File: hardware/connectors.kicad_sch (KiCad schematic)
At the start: 23 parts, among them J1 Kenwood-2.5, J10 UART, J11 Radio_Opt, J12 Speaker, J13 8P8C_Shielded, J2 USB_C, J301 +12V, J5 Kenwood-3.5, J7 Radio, J9 STLink, U3 USBLC6-2

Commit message: Modified components references
Modified references to fit the previous references (from before adding the new sheets)
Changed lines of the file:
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@@
   (symbol (lib_id "Connector:8P8C_Shielded") (at 70.485 43.815 0) (unit 1)
     (in_bom yes) (on_board yes) (dnp no) (fields_autoplaced)
-    (property "Reference" "J13" (at 70.485 26.035 0)
-      (effects (font (size 1.27 1.27)))
-    )
-    (property "Value" "8P8C_Shielded" (at 70.485 28.575 0)
+    (property "Reference" "J13" (at 70.485 26.67 0)
+      (effects (font (size 1.27 1.27)))
+    )
+    (property "Value" "8P8C_Shielded" (at 70.485 29.21 0)
       (effects (font (size 1.27 1.27)))
     )
@@
         )
         (path "/59592280-3207-432b-a891-cd517ec5cf12/7f9420e4-5dd1-4e05-8205-18dae2029540"
-          (reference "J402") (unit 1)
+          (reference "J13") (unit 1)
         )
       )
@@
         )
         (path "/59592280-3207-432b-a891-cd517ec5cf12/7f9420e4-5dd1-4e05-8205-18dae2029540"
-          (reference "R406") (unit 1)
+          (reference "R16") (unit 1)
         )
       )
@@
         )
         (path "/59592280-3207-432b-a891-cd517ec5cf12/7f9420e4-5dd1-4e05-8205-18dae2029540"
-          (reference "C401") (unit 1)
+          (reference "C32") (unit 1)
         )
       )
@@
         )
         (path "/59592280-3207-432b-a891-cd517ec5cf12/7f9420e4-5dd1-4e05-8205-18dae2029540"
-          (reference "R403") (unit 1)
+          (reference "R34") (unit 1)
         )
       )
@@
   (symbol (lib_id "Diode:BAT60A") (at 191.77 35.56 180) (unit 1)
     (in_bom yes) (on_board yes) (dnp no) (fields_autoplaced)
-    (property "Reference" "D9" (at 191.77 30.3234 0)
-      (effects (font (size 1.27 1.27)))
-    )
-    (property "Value" "BAT60A" (at 191.77 33.0985 0)
+    (property "Reference" "D9" (at 192.0875 29.21 0)
+      (effects (font (size 1.27 1.27)))
+    )
+    (property "Value" "BAT60A" (at 192.0875 31.75 0)
       (effects (font (size 1.27 1.27)))
     )
@@
         )
         (path "/59592280-3207-432b-a891-cd517ec5cf12/7f9420e4-5dd1-4e05-8205-18dae2029540"
-          (reference "D401") (unit 1)
+          (reference "D9") (unit 1)
         )
       )
@@
         )
         (path "/59592280-3207-432b-a891-cd517ec5cf12/7f9420e4-5dd1-4e05-8205-18dae2029540"
-          (reference "R401") (unit 1)
+          (reference "R70") (unit 1)
         )
       )
@@
   (symbol (lib_id "Connector:Barrel_Jack_Switch_Pin3Ring") (at 120.65 161.29 0) (unit 1)
     (in_bom yes) (on_board yes) (dnp no) (fields_autoplaced)
-    (property "Reference" "J301" (at 122.047 153.5134 0)
-      (effects (font (size 1.27 1.27)))
-    )
-    (property "Value" "+12V" (at 122.047 156.2885 0)
+    (property "Reference" "J301" (at 120.65 152.4 0)
+      (effects (font (size 1.27 1.27)))
+    )
+    (property "Value" "+12V" (at 120.65 154.94 0)
       (effects (font (size 1.27 1.27)))
     )
@@
         )
         (path "/59592280-3207-432b-a891-cd517ec5cf12/7f9420e4-5dd1-4e05-8205-18dae2029540"
-          (reference "J410") (unit 1)
+          (reference "J8") (unit 1)
         )
       )
@@
         )
         (path "/59592280-3207-432b-a891-cd517ec5cf12/7f9420e4-5dd1-4e05-8205-18dae2029540"
-          (reference "J401") (unit 1)
+          (reference "J7") (unit 1)
         )
       )
@@
         )
         (path "/59592280-3207-432b-a891-cd517ec5cf12/7f9420e4-5dd1-4e05-8205-18dae2029540"
-          (reference "R404") (unit 1)
+          (reference "R35") (unit 1)
         )
       )
@@
   (symbol (lib_id "Connector_Generic:Conn_01x03") (at 180.34 129.54 0) (unit 1)
     (in_bom no) (on_board yes) (dnp yes) (fields_autoplaced)
-    (property "Reference" "J10" (at 182.3721 128.6315 0)
+    (property "Reference" "J10" (at 182.88 128.27 0)
       (effects (font (size 1.27 1.27)) (justify left))
     )
-    (property "Value" "UART" (at 182.3721 131.4066 0)
+    (property "Value" "UART" (at 182.88 130.81 0)
       (effects (font (size 1.27 1.27)) (justify left))
     )
@@
         )
         (path "/59592280-3207-432b-a891-cd517ec5cf12/7f9420e4-5dd1-4e05-8205-18dae2029540"
-          (reference "J409") (unit 1)
+          (reference "J10") (unit 1)
         )
       )
@@
   (symbol (lib_id "Connector_Generic:Conn_01x06") (at 109.22 109.22 0) (unit 1)
     (in_bom yes) (on_board yes) (dnp no) (fields_autoplaced)
-    (property "Reference" "J11" (at 111.76 109.2199 0)
+    (property "Reference" "J11" (at 111.76 109.22 0)
       (effects (font (size 1.27 1.27)) (justify left))
     )
-    (property "Value" "Radio_Opt" (at 111.76 111.7599 0)
+    (property "Value" "Radio_Opt" (at 111.76 111.76 0)
       (effects (font (size 1.27 1.27)) (justify left))
     )
@@
         )
         (path "/59592280-3207-432b-a891-cd517ec5cf12/7f9420e4-5dd1-4e05-8205-18dae2029540"
-          (reference "J405") (unit 1)
+          (reference "J11") (unit 1)
         )
       )
@@
         )
         (path "/59592280-3207-432b-a891-cd517ec5cf12/7f9420e4-5dd1-4e05-8205-18dae2029540"
-          (reference "J403") (unit 1)
+          (reference "J1") (unit 1)
         )
       )
@@
         )
         (path "/59592280-3207-432b-a891-cd517ec5cf12/7f9420e4-5dd1-4e05-8205-18dae2029540"
-          (reference "R407") (unit 1)
+          (reference "R28") (unit 1)
         )
       )
@@
   (symbol (lib_id "Connector_Generic:Conn_01x02") (at 61.595 149.225 0) (unit 1)
     (in_bom no) (on_board yes) (dnp yes) (fields_autoplaced)
-    (property "Reference" "J12" (at 64.135 149.2249 0)
+    (property "Reference" "J12" (at 64.77 149.225 0)
       (effects (font (size 1.27 1.27)) (justify left))
     )
-    (property "Value" "Speaker" (at 64.135 151.7649 0)
+    (property "Value" "Speaker" (at 64.77 151.765 0)
       (effects (font (size 1.27 1.27)) (justify left))
     )
@@
         )
         (path "/59592280-3207-432b-a891-cd517ec5cf12/7f9420e4-5dd1-4e05-8205-18dae2029540"
-          (reference "J407") (unit 1)
+          (reference "J12") (unit 1)
         )
       )
@@
         )
         (path "/59592280-3207-432b-a891-cd517ec5cf12/7f9420e4-5dd1-4e05-8205-18dae2029540"
-          (reference "R408") (unit 1)
+          (reference "R29") (unit 1)
         )
       )
@@
   (symbol (lib_id "Connector_Generic:Conn_01x04") (at 180.34 109.22 0) (unit 1)
     (in_bom no) (on_board yes) (dnp yes) (fields_autoplaced)
-    (property "Reference" "J9" (at 182.3721 109.5815 0)
+    (property "Reference" "J9" (at 182.88 109.22 0)
       (effects (font (size 1.27 1.27)) (justify left))
     )
-    (property "Value" "STLink" (at 182.3721 112.3566 0)
+    (property "Value" "STLink" (at 182.88 111.76 0)
       (effects (font (size 1.27 1.27)) (justify left))
     )
@@
         )
         (path "/59592280-3207-432b-a891-cd517ec5cf12/7f9420e4-5dd1-4e05-8205-18dae2029540"
-          (reference "J408") (unit 1)
+          (reference "J9") (unit 1)
         )
       )
@@
         )
         (path "/59592280-3207-432b-a891-cd517ec5cf12/7f9420e4-5dd1-4e05-8205-18dae2029540"
-          (reference "U401") (unit 1)
+          (reference "U3") (unit 1)
         )
       )
@@
         )
         (path "/59592280-3207-432b-a891-cd517ec5cf12/7f9420e4-5dd1-4e05-8205-18dae2029540"
-          (reference "J404") (unit 1)
+          (reference "J5") (unit 1)
         )
       )
@@
         )
         (path "/59592280-3207-432b-a891-cd517ec5cf12/7f9420e4-5dd1-4e05-8205-18dae2029540"
-          (reference "J406") (unit 1)
+          (reference "J2") (unit 1)
         )
       )
@@
         )
         (path "/59592280-3207-432b-a891-cd517ec5cf12/7f9420e4-5dd1-4e05-8205-18dae2029540"
-          (reference "R405") (unit 1)
+          (reference "R15") (unit 1)
         )
       )
@@
         )
         (path "/59592280-3207-432b-a891-cd517ec5cf12/7f9420e4-5dd1-4e05-8205-18dae2029540"
-          (reference "R409") (unit 1)
+          (reference "R4") (unit 1)
         )
       )
@@
         )
         (path "/59592280-3207-432b-a891-cd517ec5cf12/7f9420e4-5dd1-4e05-8205-18dae2029540"
-          (reference "R410") (unit 1)
+          (reference "R3") (unit 1)
         )
       )
@@
         )
         (path "/59592280-3207-432b-a891-cd517ec5cf12/7f9420e4-5dd1-4e05-8205-18dae2029540"
-          (reference "R402") (unit 1)
-        )
-      )
+          (reference "R69") (unit 1)
+        )
+      )

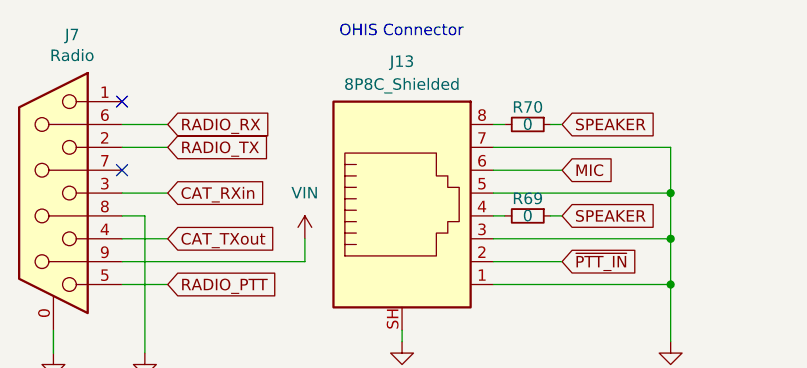
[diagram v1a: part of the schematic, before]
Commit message: Picked 8P8C reference
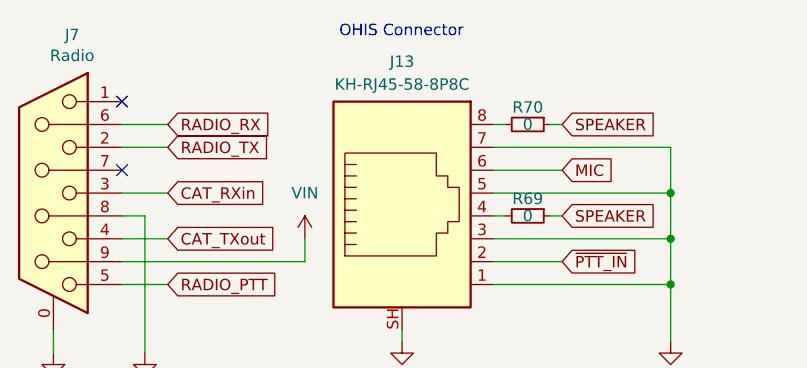
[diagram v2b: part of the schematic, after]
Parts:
- J13: value 8P8C_Shielded -> KH-RJ45-58-8P8C; footprint (none) -> M17-SmartMic:KH-RJ45-58-8P8C; LCSC Part # (none) -> C2683360; MPN (none) -> KH-RJ45-58-8P8C
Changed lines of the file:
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@@
       (effects (font (size 1.27 1.27)))
     )
-    (property "Value" "8P8C_Shielded" (at 70.485 29.21 0)
+    (property "Value" "KH-RJ45-58-8P8C" (at 70.485 29.21 0)
       (effects (font (size 1.27 1.27)))
     )
-    (property "Footprint" "" (at 70.485 43.18 90)
+    (property "Footprint" "M17-SmartMic:KH-RJ45-58-8P8C" (at 70.485 43.18 90)
       (effects (font (size 1.27 1.27)) hide)
     )
@@
       (effects (font (size 1.27 1.27)) hide)
     )
+    (property "LCSC Part #" "C2683360" (at 70.485 43.815 0)
+      (effects (font (size 1.27 1.27)) hide)
+    )
+    (property "MPN" "KH-RJ45-58-8P8C" (at 70.485 43.815 0)
+      (effects (font (size 1.27 1.27)) hide)
+    )

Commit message: Switched to M17_kicad_library for custom symbols/footprints
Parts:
- J1: footprint M17-SmartMic:PJ-211A -> M17_connectors:PJ-211A
- J13: footprint M17-SmartMic:KH-RJ45-58-8P8C -> M17_connectors:KH-RJ45-58-8P8C
- J5: footprint M17-SmartMic:PJ-3136-B -> M17_connectors:PJ-3136-B
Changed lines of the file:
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@@
       (effects (font (size 1.27 1.27)))
     )
-    (property "Footprint" "M17-SmartMic:KH-RJ45-58-8P8C" (at 70.485 43.18 90)
+    (property "Footprint" "M17_connectors:KH-RJ45-58-8P8C" (at 70.485 43.18 90)
       (effects (font (size 1.27 1.27)) hide)
     )
@@
       (effects (font (size 1.27 1.27)))
     )
-    (property "Footprint" "M17-SmartMic:PJ-211A" (at 46.99 85.725 0)
-      (effects (font (size 1.27 1.27)) hide)
-    )
-    (property "Datasheet" "SJ1-2503A" (at 46.99 85.725 0)
+    (property "Footprint" "M17_connectors:PJ-211A" (at 46.99 85.725 0)
+      (effects (font (size 1.27 1.27)) hide)
+    )
+    (property "Datasheet" "" (at 46.99 85.725 0)
       (effects (font (size 1.27 1.27)) hide)
     )
@@
       (effects (font (size 1.27 1.27)))
     )
-    (property "Footprint" "M17-SmartMic:PJ-3136-B" (at 46.99 114.935 0)
-      (effects (font (size 1.27 1.27)) hide)
-    )
+    (property "Footprint" "M17_connectors:PJ-3136-B" (at 46.99 114.935 0)
+      (effects (font (size 1.27 1.27)) hide)
+    )

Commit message: Updated various MPNs
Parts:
- R70: MPN Generic R/2k2/0603 -> Generic R/0R/0603
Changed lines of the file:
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@@
       (effects (font (size 1.524 1.524)))
     )
-    (property "MPN" "Generic R/2k2/0603" (at 84.455 33.655 0)
+    (property "MPN" "Generic R/0R/0603" (at 84.455 33.655 0)
       (effects (font (size 1.27 1.27)) hide)
     )

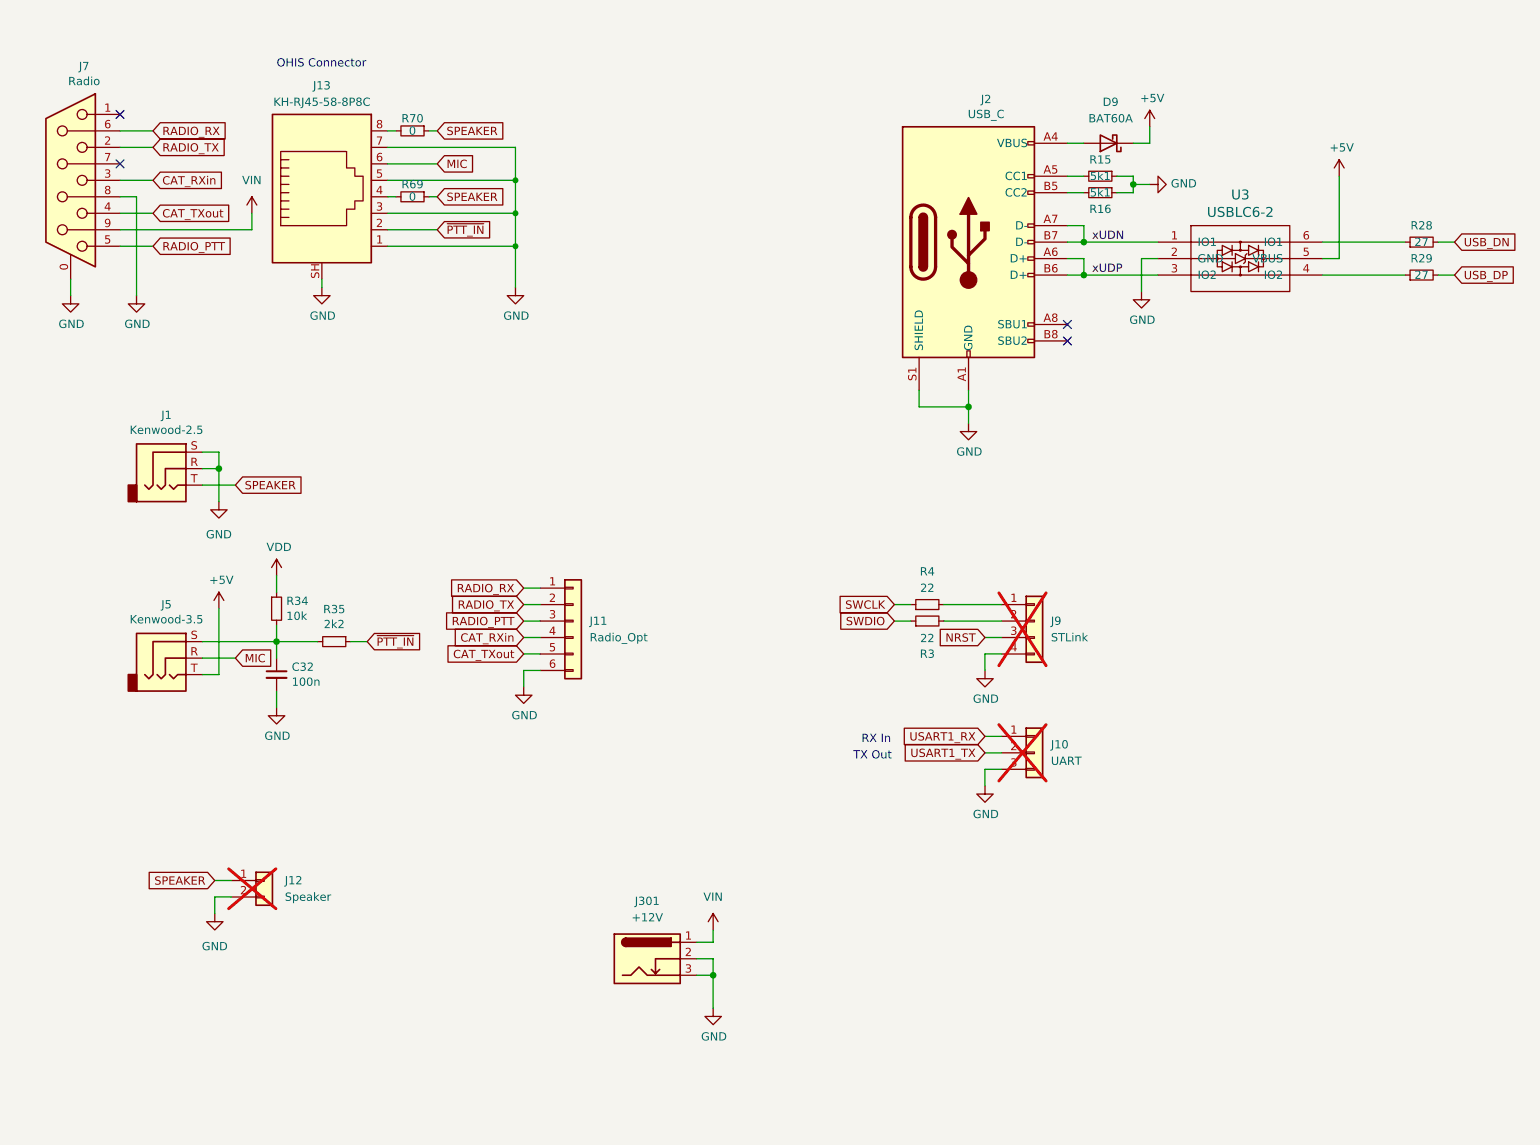
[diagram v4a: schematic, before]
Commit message: Reworked schematic
Rearranged disposition and renumbered components
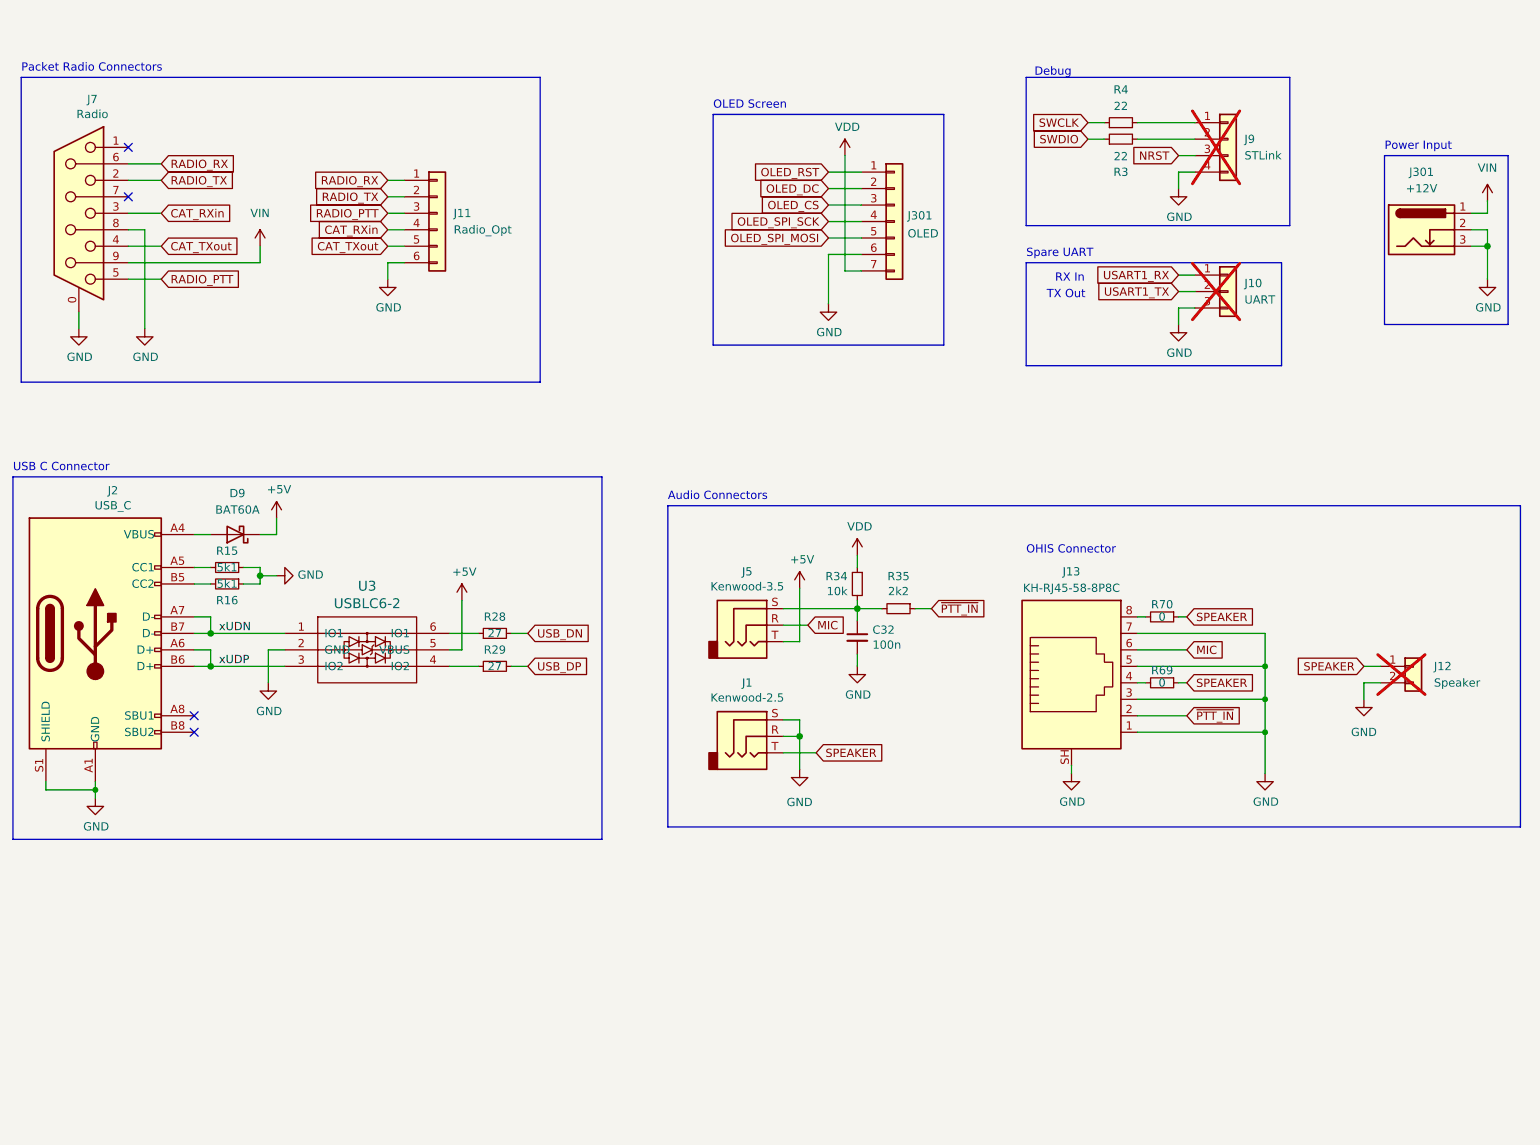
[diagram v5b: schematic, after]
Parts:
- added J301: OLED, Connector_PinHeader_2.54mm:PinHeader_1x07_P2.54mm_Vertical, symbol Connector_Generic:Conn_01x07
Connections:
- net GND: now also J301.6 (Pin_6)
- net VDD: now also J301.7 (Pin_7)
- new net OLED_CS: J301.3 (Pin_3)
- new net OLED_DC: J301.2 (Pin_2)
- new net OLED_RST: J301.1 (Pin_1)
- new net OLED_SPI_MOSI: J301.5 (Pin_5)
- new net OLED_SPI_SCK: J301.4 (Pin_4)
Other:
- note added: "Audio Connectors"
- note added: "Debug"
- note added: "OLED Screen"
- note added: "Packet Radio Connectors"
- note added: "Power Input"
- note added: "Spare UART"
- note added: "USB C Connector"
- moved on the sheet: C32, D9, J1, J10, J11, J12, J13, J2, J301, J5, J7, J9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
